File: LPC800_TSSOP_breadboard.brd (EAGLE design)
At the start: 30.5 x 17.7 mm, 16 parts, among them Q1 12MHz

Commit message: * small fixes on TODO list
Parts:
- added C6: (no value), SquantorRCL:C0603K
- C2, C3: device bart_rcl:C0603 -> SquantorRCL:C0603K
- moved LOGO1 11.3 mm to (20.2, 6.45), turned to 0 degrees
- moved Q1 2.04 mm to (23.4, 11.5)
- moved C4 2.04 mm to (5.00, 10.8)
- moved R2 2.04 mm to (8.81, 10.8)
- moved U$2 2.04 mm to (5.00, 7.98)
- moved U$4 2.04 mm to (7.54, 6.07)
- moved C5 2.04 mm to (5.00, 5.12)
- moved R1 2.04 mm to (8.81, 5.12)
- moved JP1 2.04 mm to (17.1, 14.3)
- moved U$3 2.04 mm to (7.54, 11.2)
- moved JP2 2.04 mm to (17.1, 1.63)
- moved C1 2.04 mm to (18.3, 13.1)
- moved JP3 2.04 mm to (27.5, 7.98)
- moved U$1 2.04 mm to (18.3, 7.98)
- moved C2 1.85 mm to (21.2, 8.27)
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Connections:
- net VDD: now also C6.1
- net VSS: now also C6.2
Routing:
- net VSS: track 53.3 -> 48.3 mm
- net VDD: track 44.8 -> 48.4 mm
- net PIO0_5: track 35.5 -> 36.2 mm
- net PIO0_8: track 11.5 -> 10.9 mm
- net PIO0_9: track 12.9 -> 12.2 mm
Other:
- board size 30.5 x 17.7 mm -> 31.4 x 15.8 mm

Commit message: * doing some TODO's
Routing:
- net VSS: track 48.3 -> 48.6 mm, vias 2 -> 3
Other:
- board text added: "V 2014.04.15"
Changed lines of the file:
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@@
 <wire x1="30.48" y1="17.6784" x2="30.48" y2="0" width="0.254" layer="102"/>
 <wire x1="30.48" y1="0" x2="0" y2="0" width="0.254" layer="102"/>
+<text x="29.8704" y="12.192" size="1.016" layer="22" rot="MR270">V 2014.04.15</text>
 </plain>
 <attributes>
@@
 <via x="27.5844" y="6.7056" extent="1-16" drill="0.4" shape="octagon"/>
 <wire x1="27.5844" y1="6.7056" x2="27.7368" y2="7.9248" width="0.6096" layer="1"/>
-<wire x1="27.7368" y1="7.9248" x2="27.7368" y2="10.0584" width="0.6096" layer="1"/>
+<wire x1="27.7368" y1="7.9248" x2="27.7368" y2="10.3632" width="0.6096" layer="1"/>
 <wire x1="27.5844" y1="6.7056" x2="29.4513" y2="6.7056" width="0.6096" layer="1"/>
 <wire x1="29.4513" y1="7.9756" x2="27.7368" y2="7.9248" width="0.6096" layer="1"/>
@@
 </polygon>
 <contactref element="C6" pad="2"/>
+<via x="15.3924" y="9.4488" extent="1-16" drill="0.4" shape="octagon"/>
 </signal>
 <signal name="VDD">
@@
 <wire x1="18.6563" y1="10.8859" x2="18.6638" y2="10.8934" width="0.3048" layer="1"/>
 <wire x1="29.4513" y1="5.4356" x2="29.4513" y2="4.4831" width="0.6096" layer="1"/>
-<wire x1="29.4513" y1="4.4831" x2="29.1338" y2="4.1656" width="0.6096" layer="1"/>
-<via x="29.1338" y="4.1656" extent="1-16" drill="0.4" shape="octagon"/>
-<wire x1="29.1338" y1="4.1656" x2="16.256" y2="4.1656" width="0.6096" layer="16"/>
+<via x="27.0002" y="4.1656" extent="1-16" drill="0.4" shape="octagon"/>
+<wire x1="27.0002" y1="4.1656" x2="16.256" y2="4.1656" width="0.6096" layer="16"/>
 <wire x1="12.192" y1="8.2296" x2="16.256" y2="4.1656" width="0.6096" layer="16"/>
 <contactref element="C6" pad="1"/>
@@
 <wire x1="6.3373" y1="8.2296" x2="7.8613" y2="8.2296" width="0.6096" layer="16"/>
 <wire x1="7.8613" y1="8.2296" x2="12.192" y2="8.2296" width="0.6096" layer="16"/>
+<wire x1="29.4513" y1="4.4831" x2="29.1338" y2="4.1656" width="0.6096" layer="1"/>
+<wire x1="29.1338" y1="4.1656" x2="27.0002" y2="4.1656" width="0.6096" layer="1"/>
 </signal>
 <signal name="PIO0_0">

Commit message: * updated board and schem with todo's
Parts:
- removed JP1, JP2: (no value), bart_connectors:1X11_SMALL
- removed LOGO1: OSHW_LOGO_FILLX0150-NT, ohw-logo:OSHW_FILLX150_NOTEXT
- added JP4, JP5: (no value), SquantorConnectors:1X12_SMALL
- added LOGO2: OSHW_LOGO_FILLX0150-NT, ohw-logo:OSHW_FILLX150_NOTEXT
- C4, C5: device bart_rcl:C0805 -> bart_rcl:C0805K
- moved C5 7.07 mm to (2.54, 11.7), turned to 180 degrees
- moved C4 6.55 mm to (2.54, 4.76), turned to 180 degrees
- moved U$2 2.76 mm to (2.30, 8.53), turned to 0 degrees
- moved U$3 2.56 mm to (6.35, 8.89)
- moved U$4 1.55 mm to (6.35, 5.08)
- moved R2 0.87 mm to (8.26, 10.2)
- moved C2 0.71 mm to (20.6, 8.59)
- moved C3 0.71 mm to (25.0, 8.59)
- moved C6 0.71 mm to (13.4, 8.83)
- moved C1 0.71 mm to (17.7, 12.7)
- moved JP3 0.71 mm to (26.9, 7.66)
- moved U$1 0.71 mm to (17.7, 7.66)
- moved Q1 0.64 mm to (22.8, 11.5)
- moved R1 0.56 mm to (8.26, 5.08)
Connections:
- net PIO0_0: now also JP4.9; no longer JP1.9
- net PIO0_1: now also JP4.2; no longer JP1.2
- net PIO0_10: now also JP5.11; no longer JP2.10
- net PIO0_11: now also JP5.10; no longer JP2.9
- net PIO0_12: now also JP5.5; no longer JP2.4
- net PIO0_13: now also JP5.4; no longer JP2.3
- net PIO0_14: now also JP4.10; no longer JP1.10
- net PIO0_15: now also JP4.1; no longer JP1.1
- net PIO0_16: now also JP5.12; no longer JP2.11
- net PIO0_17: now also JP5.3; no longer JP2.2
- net PIO0_2: now also JP5.9; no longer JP2.8
- net PIO0_3: now also JP5.8; no longer JP2.7
- net PIO0_4: now also JP5.7; no longer JP2.6
- net PIO0_5: now also JP5.6; no longer JP2.5
- net PIO0_6: now also JP4.8; no longer JP1.8
- net PIO0_7: now also JP4.7; no longer JP1.7
- net PIO0_8: now also JP4.4; no longer JP1.4
- net PIO0_9: now also JP4.3; no longer JP1.3
- net VCCIO: now also JP4.12; no longer JP2.1
- net VDD: now also JP4.5, JP5.1; no longer JP1.5
- net VSS: now also JP4.11, JP4.6, JP5.2; no longer JP1.11, JP1.6
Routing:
- net VSS: track 48.6 -> 19.8 mm, vias 3 -> 4
- net VDD: track 48.4 -> 56.0 mm
- net PIO0_5: track 36.2 -> 33.9 mm
- net VCCIO: track 6.74 -> 5.31 mm
- net PIO0_12: track 22.3 -> 21.2 mm
- net PIO0_8: track 10.9 -> 9.92 mm
- net PIO0_9: track 12.2 -> 11.6 mm
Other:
- board size 31.4 x 15.8 mm -> 30.5 x 15.2 mm

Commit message: * small beautification mods
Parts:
- moved LOGO2 3.86 mm to (18.3, 3.59)
- moved U$3 0.71 mm to (6.67, 9.53)
- moved U$4 0.71 mm to (6.67, 5.71)
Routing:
- net PIO0_5: track 33.9 -> 34.6 mm
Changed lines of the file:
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@@
 <setting verticaltext="up"/>
 </settings>
-<grid distance="0.635" unitdist="mm" unit="mm" style="lines" multiple="1" display="yes" altdistance="0.635" altunitdist="mm" altunit="mm"/>
+<grid distance="12.5" unitdist="mil" unit="mil" style="lines" multiple="1" display="yes" altdistance="0.635" altunitdist="mm" altunit="mm"/>
 <layers>
 <layer number="1" name="Top" color="4" fill="1" visible="yes" active="yes"/>
@@
 <layer number="17" name="Pads" color="2" fill="1" visible="yes" active="yes"/>
 <layer number="18" name="Vias" color="2" fill="1" visible="yes" active="yes"/>
-<layer number="19" name="Unrouted" color="6" fill="1" visible="no" active="yes"/>
+<layer number="19" name="Unrouted" color="6" fill="1" visible="yes" active="yes"/>
 <layer number="20" name="Dimension" color="15" fill="1" visible="yes" active="yes"/>
 <layer number="21" name="tPlace" color="7" fill="1" visible="yes" active="yes"/>
@@
 <attribute name="NAME" x="7.1628" y="12.5984" size="1.016" layer="26" rot="MR180"/>
 </element>
-<element name="U$3" library="bart_btn" package="KMR2" value="RESET" x="6.35" y="8.89" smashed="yes" rot="R90">
-<attribute name="VALUE" x="8.89" y="12.065" size="1.016" layer="21" rot="R180"/>
-</element>
-<element name="U$4" library="bart_btn" package="KMR2" value="ISP" x="6.35" y="5.08" smashed="yes" rot="R270">
-<attribute name="VALUE" x="10.3124" y="3.2258" size="1.016" layer="21" rot="R90"/>
+<element name="U$3" library="bart_btn" package="KMR2" value="RESET" x="6.6675" y="9.525" smashed="yes" rot="R90">
+<attribute name="VALUE" x="9.2075" y="12.3825" size="1.016" layer="21" rot="R180"/>
+</element>
+<element name="U$4" library="bart_btn" package="KMR2" value="ISP" x="6.6675" y="5.715" smashed="yes" rot="R270">
+<attribute name="VALUE" x="10.6299" y="3.8608" size="1.016" layer="21" rot="R90"/>
 </element>
 <element name="C6" library="SquantorRCL" package="C0603K" value="" x="13.3858" y="8.8265" smashed="yes" rot="R90">
@@
 <attribute name="VALUE" x="0" y="-1.905" size="1.27" layer="27"/>
 </element>
-<element name="LOGO2" library="ohw-logo" package="OSHW_FILLX150_NOTEXT" value="OSHW_LOGO_FILLX0150-NT" x="17.653" y="7.4041" rot="MR0"/>
+<element name="LOGO2" library="ohw-logo" package="OSHW_FILLX150_NOTEXT" value="OSHW_LOGO_FILLX0150-NT" x="18.288" y="3.5941" rot="MR0"/>
 </elements>
 <signals>
@@
 <contactref element="R1" pad="1"/>
 <contactref element="R2" pad="1"/>
-<wire x1="7.2263" y1="10.4131" x2="7.405" y2="10.16" width="0.6096" layer="16"/>
-<wire x1="7.2263" y1="8.5725" x2="7.2263" y2="7.9375" width="0.6096" layer="16"/>
-<via x="11.557" y="7.9121" extent="1-16" drill="0.4" shape="octagon"/>
 <wire x1="18.0213" y1="10.5684" x2="18.0288" y2="10.5759" width="0.3048" layer="1"/>
 <wire x1="28.8163" y1="5.1181" x2="28.8163" y2="4.1656" width="0.6096" layer="1"/>
 <via x="26.3652" y="3.8481" extent="1-16" drill="0.4" shape="octagon"/>
-<wire x1="26.3652" y1="3.8481" x2="15.621" y2="3.8481" width="0.6096" layer="16"/>
-<wire x1="11.557" y1="7.9121" x2="15.621" y2="3.8481" width="0.6096" layer="16"/>
+<wire x1="26.3652" y1="3.8481" x2="15.5194" y2="3.8481" width="0.6096" layer="16"/>
 <contactref element="C6" pad="1"/>
 <wire x1="13.3858" y1="7.9515" x2="17.0828" y2="7.9515" width="0.6096" layer="1"/>
@@
 <wire x1="17.9578" y1="8.8265" x2="18.0288" y2="8.8975" width="0.3048" layer="1"/>
 <wire x1="18.0288" y1="8.8975" x2="18.0288" y2="10.5759" width="0.3048" layer="1"/>
-<wire x1="11.557" y1="7.9121" x2="11.5964" y2="7.9515" width="0.6096" layer="1"/>
-<wire x1="11.5964" y1="7.9515" x2="13.3858" y2="7.9515" width="0.6096" layer="1"/>
 <wire x1="28.8163" y1="4.1656" x2="28.4988" y2="3.8481" width="0.6096" layer="1"/>
 <wire x1="28.4988" y1="3.8481" x2="26.3652" y2="3.8481" width="0.6096" layer="1"/>
@@
 <wire x1="1.54" y1="4.7625" x2="1.27" y2="4.7625" width="0.6096" layer="16"/>
 <wire x1="1.27" y1="7.3844" x2="1.3487" y2="7.3844" width="0.6096" layer="16"/>
-<wire x1="7.2263" y1="8.5725" x2="1.5875" y2="8.5725" width="0.6096" layer="16"/>
 <wire x1="1.5875" y1="8.5725" x2="1.27" y2="8.255" width="0.6096" layer="16"/>
 <wire x1="1.27" y1="8.255" x2="1.27" y2="7.4631" width="0.6096" layer="16"/>
 <wire x1="1.27" y1="7.4631" x2="1.3487" y2="7.3844" width="0.6096" layer="16"/>
-<wire x1="11.557" y1="7.9121" x2="7.2517" y2="7.9121" width="0.6096" layer="16"/>
-<wire x1="7.2517" y1="7.9121" x2="7.2263" y2="7.9375" width="0.6096" layer="16"/>
-<wire x1="7.2517" y1="7.9121" x2="7.2517" y2="5.2333" width="0.6096" layer="16"/>
-<wire x1="7.2517" y1="5.2333" x2="7.405" y2="5.08" width="0.6096" layer="16"/>
-<wire x1="7.2263" y1="8.5725" x2="7.2263" y2="9.9813" width="0.6096" layer="16"/>
-<wire x1="7.2263" y1="9.9813" x2="7.405" y2="10.16" width="0.6096" layer="16"/>
+<wire x1="7.405" y1="5.08" x2="7.405" y2="7.9375" width="0.6096" layer="16"/>
+<wire x1="7.405" y1="7.9375" x2="7.405" y2="8.5725" width="0.6096" layer="16"/>
+<wire x1="7.405" y1="8.5725" x2="7.405" y2="10.16" width="0.6096" layer="16"/>
+<wire x1="13.3858" y1="7.9515" x2="13.3858" y2="7.9375" width="0.6096" layer="1"/>
+<wire x1="13.3858" y1="7.9375" x2="11.43" y2="7.9375" width="0.6096" layer="1"/>
+<via x="11.43" y="7.9375" extent="1-16" drill="0.4" shape="octagon"/>
+<wire x1="11.43" y1="7.9375" x2="7.405" y2="7.9375" width="0.6096" layer="16"/>
+<wire x1="1.5875" y1="8.5725" x2="7.405" y2="8.5725" width="0.6096" layer="16"/>
+<wire x1="15.5194" y1="3.8481" x2="11.43" y2="7.9375" width="0.6096" layer="16"/>
 </signal>
 <signal name="PIO0_0">
@@
 <wire x1="16.7513" y1="6.3881" x2="16.4338" y2="6.3881" width="0.3048" layer="1"/>
 <wire x1="16.4338" y1="6.3881" x2="15.7988" y2="7.0231" width="0.3048" layer="1"/>
-<wire x1="15.7988" y1="7.0231" x2="11.0871" y2="7.0231" width="0.3048" layer="1"/>
+<wire x1="15.7988" y1="7.0231" x2="10.7569" y2="7.0231" width="0.3048" layer="1"/>
 <contactref element="JP5" pad="6"/>
 <wire x1="16.7288" y1="3.3938" x2="15.875" y2="2.54" width="0.3048" layer="1"/>
 <wire x1="15.875" y1="2.54" x2="15.24" y2="2.54" width="0.3048" layer="1"/>
 <wire x1="15.24" y1="2.54" x2="13.97" y2="1.27" width="0.3048" layer="1"/>
-<wire x1="11.0871" y1="7.0231" x2="9.9702" y2="8.14" width="0.3048" layer="1"/>
-<wire x1="9.9702" y1="8.14" x2="8.35" y2="8.14" width="0.3048" layer="1"/>
-<wire x1="8.35" y1="8.14" x2="4.35" y2="8.14" width="0.3048" layer="1"/>
+<wire x1="8.6675" y1="8.775" x2="4.6675" y2="8.775" width="0.3048" layer="1"/>
 <wire x1="9.105" y1="10.16" x2="9.525" y2="10.16" width="0.3048" layer="16"/>
-<wire x1="9.525" y1="10.16" x2="10.16" y2="9.525" width="0.3048" layer="16"/>
-<via x="10.16" y="9.525" extent="1-16" drill="0.4" shape="octagon"/>
-<wire x1="10.16" y1="9.525" x2="10.16" y2="8.3298" width="0.3048" layer="1"/>
-<wire x1="10.16" y1="8.3298" x2="9.9702" y2="8.14" width="0.3048" layer="1"/>
+<wire x1="10.7569" y1="7.0231" x2="10.16" y2="7.62" width="0.3048" layer="1"/>
+<wire x1="10.16" y1="7.62" x2="10.16" y2="8.89" width="0.3048" layer="1"/>
+<via x="10.16" y="10.16" extent="1-16" drill="0.4" shape="octagon"/>
+<wire x1="10.16" y1="8.89" x2="10.16" y2="10.16" width="0.3048" layer="1"/>
+<wire x1="10.16" y1="10.16" x2="9.105" y2="10.16" width="0.3048" layer="16"/>
+<wire x1="8.6675" y1="8.775" x2="10.045" y2="8.775" width="0.3048" layer="1"/>
+<wire x1="10.045" y1="8.775" x2="10.16" y2="8.89" width="0.3048" layer="1"/>
 </signal>
 <signal name="PIO0_6">
@@
 <wire x1="15.4813" y1="3.2131" x2="13.3731" y2="3.2131" width="0.3048" layer="1"/>
 <wire x1="13.3731" y1="3.2131" x2="11.43" y2="1.27" width="0.3048" layer="1"/>
-<wire x1="16.0788" y1="5.4731" x2="15.7219" y2="5.83" width="0.3048" layer="1"/>
-<wire x1="15.7219" y1="5.83" x2="11.43" y2="5.83" width="0.3048" layer="1"/>
-<wire x1="10.795" y1="5.83" x2="8.35" y2="5.83" width="0.3048" layer="1"/>
-<wire x1="4.35" y1="5.83" x2="8.35" y2="5.83" width="0.3048" layer="1"/>
-<wire x1="9.105" y1="5.08" x2="10.045" y2="5.08" width="0.3048" layer="16"/>
-<wire x1="10.045" y1="5.08" x2="10.795" y2="5.83" width="0.3048" layer="16"/>
-<via x="10.795" y="5.83" extent="1-16" drill="0.4" shape="octagon"/>
-<wire x1="10.795" y1="5.83" x2="11.43" y2="5.83" width="0.3048" layer="1"/>
+<wire x1="4.6675" y1="6.465" x2="8.6675" y2="6.465" width="0.3048" layer="1"/>
+<wire x1="16.0788" y1="5.4731" x2="15.2019" y2="6.35" width="0.3048" layer="1"/>
+<wire x1="10.16" y1="6.35" x2="10.045" y2="6.465" width="0.3048" layer="1"/>
+<wire x1="10.045" y1="6.465" x2="8.6675" y2="6.465" width="0.3048" layer="1"/>
+<wire x1="9.105" y1="5.08" x2="9.8425" y2="5.08" width="0.3048" layer="16"/>
+<wire x1="9.8425" y1="5.08" x2="10.16" y2="5.3975" width="0.3048" layer="16"/>
+<wire x1="10.16" y1="5.3975" x2="10.16" y2="6.35" width="0.3048" layer="16"/>
+<via x="10.16" y="6.35" extent="1-16" drill="0.4" shape="octagon"/>
+<wire x1="10.16" y1="6.35" x2="15.2019" y2="6.35" width="0.3048" layer="1"/>
 </signal>
 <signal name="PIO0_11">

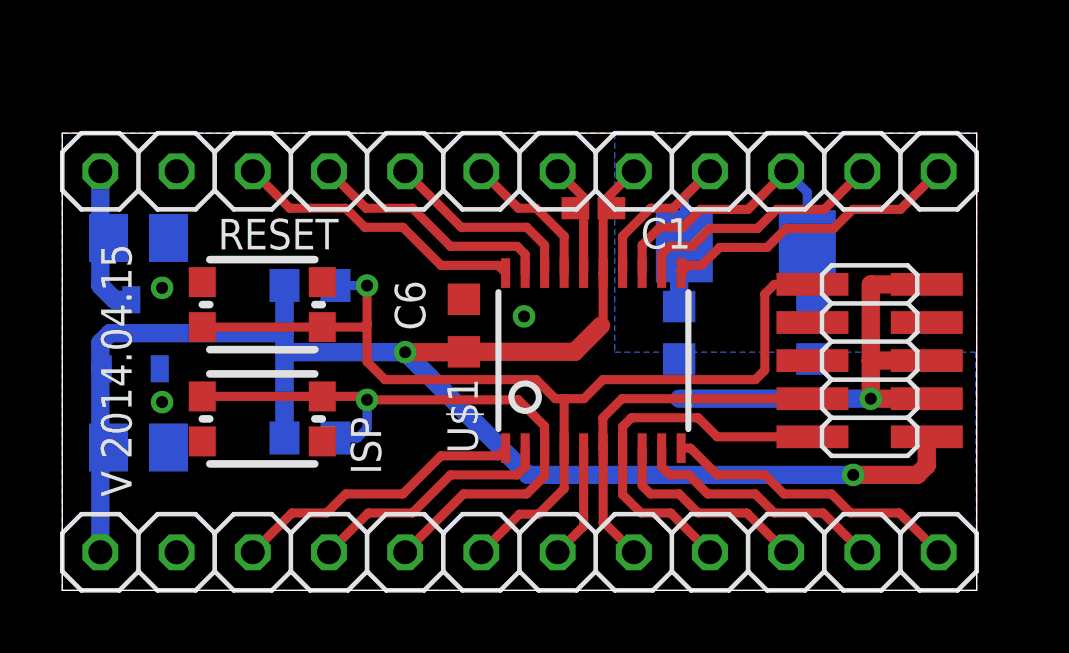
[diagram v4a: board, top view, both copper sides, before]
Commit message: * minor updates with silk, pinout documentation, hole expansion
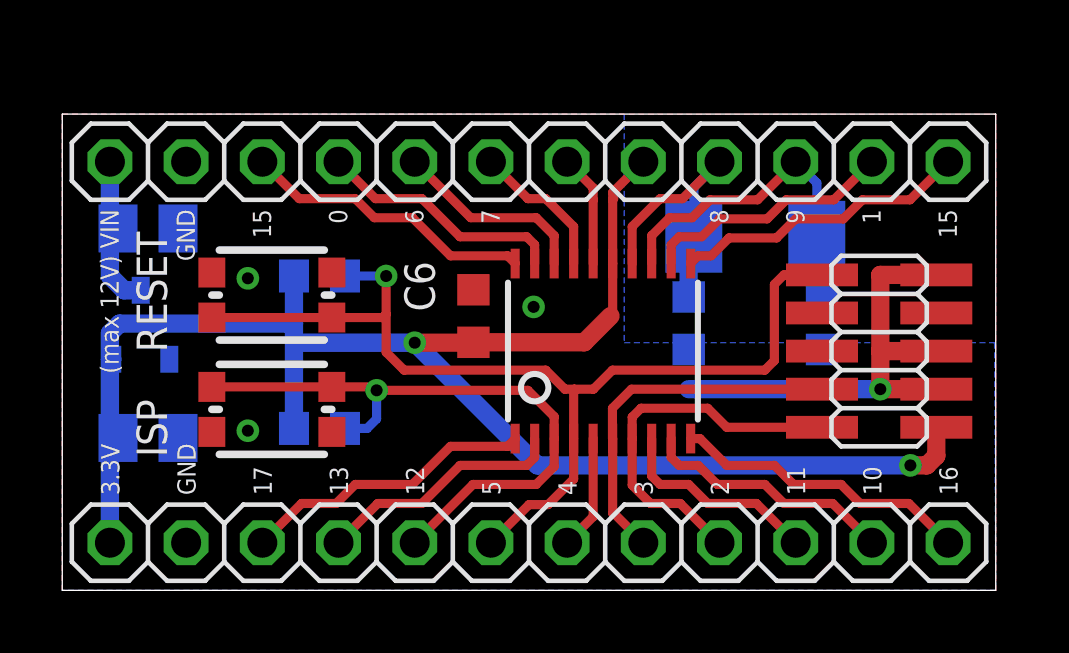
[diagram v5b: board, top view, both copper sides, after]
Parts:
- removed C1: 100n, bart_rcl:C0402K
- removed U$1: LPC812M101JDH20, LPC800:TSSOP20
- added LPC812: LPC812M101JDH20, LPC800:TSSOP20
- JP4, JP5: device SquantorConnectors:1X12_SMALL -> SquantorConnectors:1X12_NORMAL_OCT
- moved C6 0.45 mm to (13.7, 9.14)
- moved U$2 0.45 mm to (2.62, 8.85)
- moved C4 0.45 mm to (2.86, 5.08)
- moved Q1 0.45 mm to (23.1, 11.8)
- moved U$4 0.45 mm to (6.99, 6.03)
- moved C5 0.45 mm to (2.86, 12.1)
- moved JP3 0.45 mm to (27.2, 7.98)
- moved JP5 0.45 mm to (15.6, 1.59)
- moved LOGO2 0.45 mm to (18.6, 3.91)
- moved R1 0.45 mm to (8.57, 5.40)
- moved U$3 0.45 mm to (6.99, 9.84)
- moved C2 0.45 mm to (20.9, 8.90)
- moved C3 0.45 mm to (25.3, 8.90)
- moved JP4 0.45 mm to (15.6, 14.3)
- moved R2 0.45 mm to (8.57, 10.5)
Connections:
- net PIO0_0: now also LPC812.19; no longer U$1.19
- net PIO0_1: now also LPC812.12; no longer U$1.12
- net PIO0_10: now also LPC812.9; no longer U$1.9
- net PIO0_11: now also LPC812.8; no longer U$1.8
- net PIO0_12: now also LPC812.3; no longer U$1.3
- net PIO0_13: now also LPC812.2; no longer U$1.2
- net PIO0_14: now also LPC812.20; no longer U$1.20
- net PIO0_15: now also LPC812.11; no longer U$1.11
- net PIO0_16: now also LPC812.10; no longer U$1.10
- net PIO0_17: now also LPC812.1; no longer U$1.1
- net PIO0_2: now also LPC812.7; no longer U$1.7
- net PIO0_3: now also LPC812.6; no longer U$1.6
- net PIO0_4: now also LPC812.5; no longer U$1.5
- net PIO0_5: now also LPC812.4; no longer U$1.4
- net PIO0_6: now also LPC812.18; no longer U$1.18
- net PIO0_7: now also LPC812.17; no longer U$1.17
- net PIO0_8: now also LPC812.14; no longer U$1.14
- net PIO0_9: now also LPC812.13; no longer U$1.13
- net VDD: now also LPC812.15; no longer C1.1, U$1.15
- net VSS: now also LPC812.16; no longer C1.2, U$1.16
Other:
- board size 30.5 x 15.2 mm -> 31.1 x 15.9 mm
- board text added: "(max 12V) VIN"
- board text added: "0"
- board text added: "1"
- board text added: "10"
- board text added: "11"
- board text added: "12"
- board text added: "13"
- board text added: "15"
- board text added: "16"
- board text added: "17"
- board text added: "2"
- board text added: "3"
- board text added: "3.3V"
- board text added: "4"
- board text added: "5"
- board text added: "6"
- board text added: "7"
- board text added: "8"
- board text added: "9"
- board text added: "GND"
- board text added: "V2014.05.11"
- board text removed: "V 2014.04.15"

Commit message: * small modifications * improved regulator decoupling capacitor position to leave more space for the pinheaders * improved crystal positioning to leave more space for the pinheaders
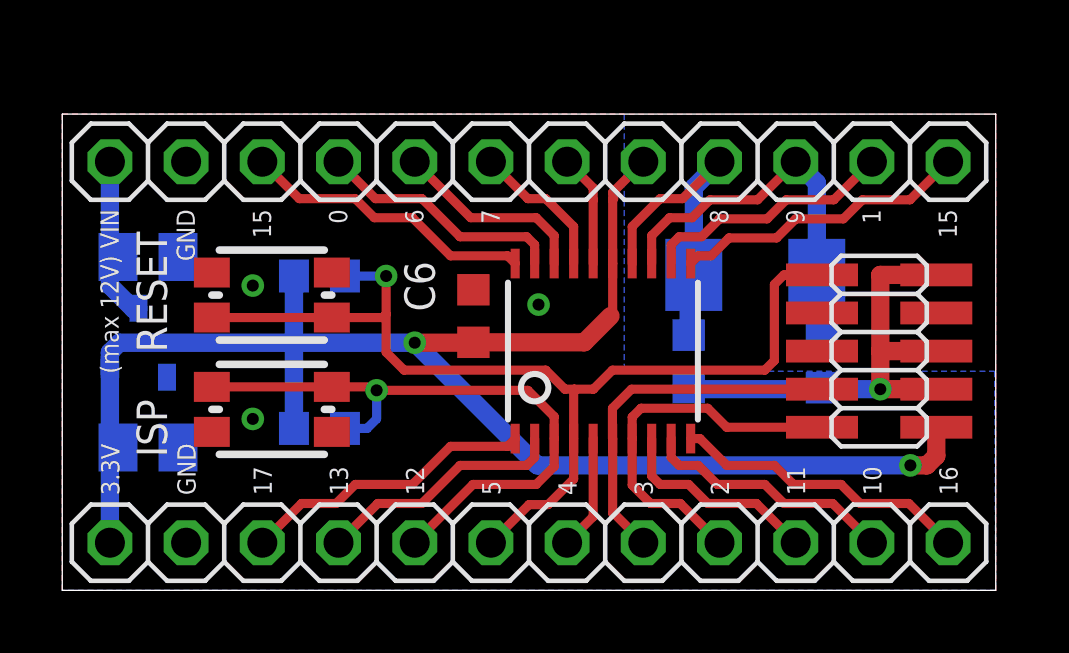
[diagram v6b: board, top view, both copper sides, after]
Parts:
- U$3, U$4: device bart_btn:KMR2 -> SquantorButtons:KMR2
- moved Q1 1.27 mm to (23.1, 10.5)
- moved C2 1.27 mm to (20.9, 7.63)
- moved C3 1.27 mm to (25.3, 7.63)
- moved C5 0.95 mm to (2.86, 11.1)
- moved U$2 0.60 mm to (2.54, 8.26)
- moved C4 0.32 mm to (2.86, 4.76)
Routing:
- net PIO0_8: track 9.92 -> 12.1 mm
- net PIO0_9: track 11.6 -> 13.8 mm
- net VDD: track 55.5 -> 56.1 mm
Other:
- board text added: "V2014.05.29"
- board text removed: "V2014.05.11"

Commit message: * finished LPC800 mini board * fixed pin 1 for JTAG connection - TODO: Printout inspection and checks for the button layout
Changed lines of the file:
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@@
 <?xml version="1.0" encoding="utf-8"?>
 <!DOCTYPE eagle SYSTEM "eagle.dtd">
-<eagle version="6.5.0">
+<eagle version="7.1.0">
 <drawing>
 <settings>
@@
 <text x="3.81" y="12.7" size="0.6096" layer="25" rot="R270">GND</text>
 <text x="1.27" y="12.7" size="0.6096" layer="25" rot="R270">(max 12V) VIN</text>
+<text x="30.48" y="3.81" size="1.778" layer="25" rot="R90">1</text>
 </plain>
 <attributes>
@@
 <pass name="Default">
 <param name="RoutingGrid" value="50mil"/>
+<param name="AutoGrid" value="1"/>
+<param name="Efforts" value="0"/>
+<param name="TopRouterVariant" value="1"/>
 <param name="tpViaShape" value="round"/>
 <param name="PrefDir.1" value="|"/>
